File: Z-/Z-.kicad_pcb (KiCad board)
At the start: 4 copper layers, 98 x 98 mm, 138 parts, among them J1 200528-0100, J2 Conn_Coaxial, J3 Conn_Coaxial, J4 200528-0100, J5 Conn_01x02, K1 IM02DGR, Q1 NX3008NBKS, Q10 NX3008NBKS, Q11 IRLML2803, Q12 MBT2222ADW1T1, Q13 IRLML2803, Q14 NX3008NBKS, Q15 IRF7404, Q16 MBT2222ADW1T1, Q17 IRF7404, Q18 IRLML2803, Q19 IRF7404, Q2 NX3008NBKS, Q3 MBT2222ADW1T1, Q4 MBT2222ADW1T1, Q5 NX3008NBKS, Q6 NX3008NBKS, Q7 MBT2222ADW1T1, Q8 MBT2222ADW1T1, Q9 MMBT2222AT, U1 OPT4003DNPRQ1, U2 LTC4316xDD, U3 ADM1176-1ARMZ-R7, U4 NCV891330PD50R2G, U5 DRV8830DRC

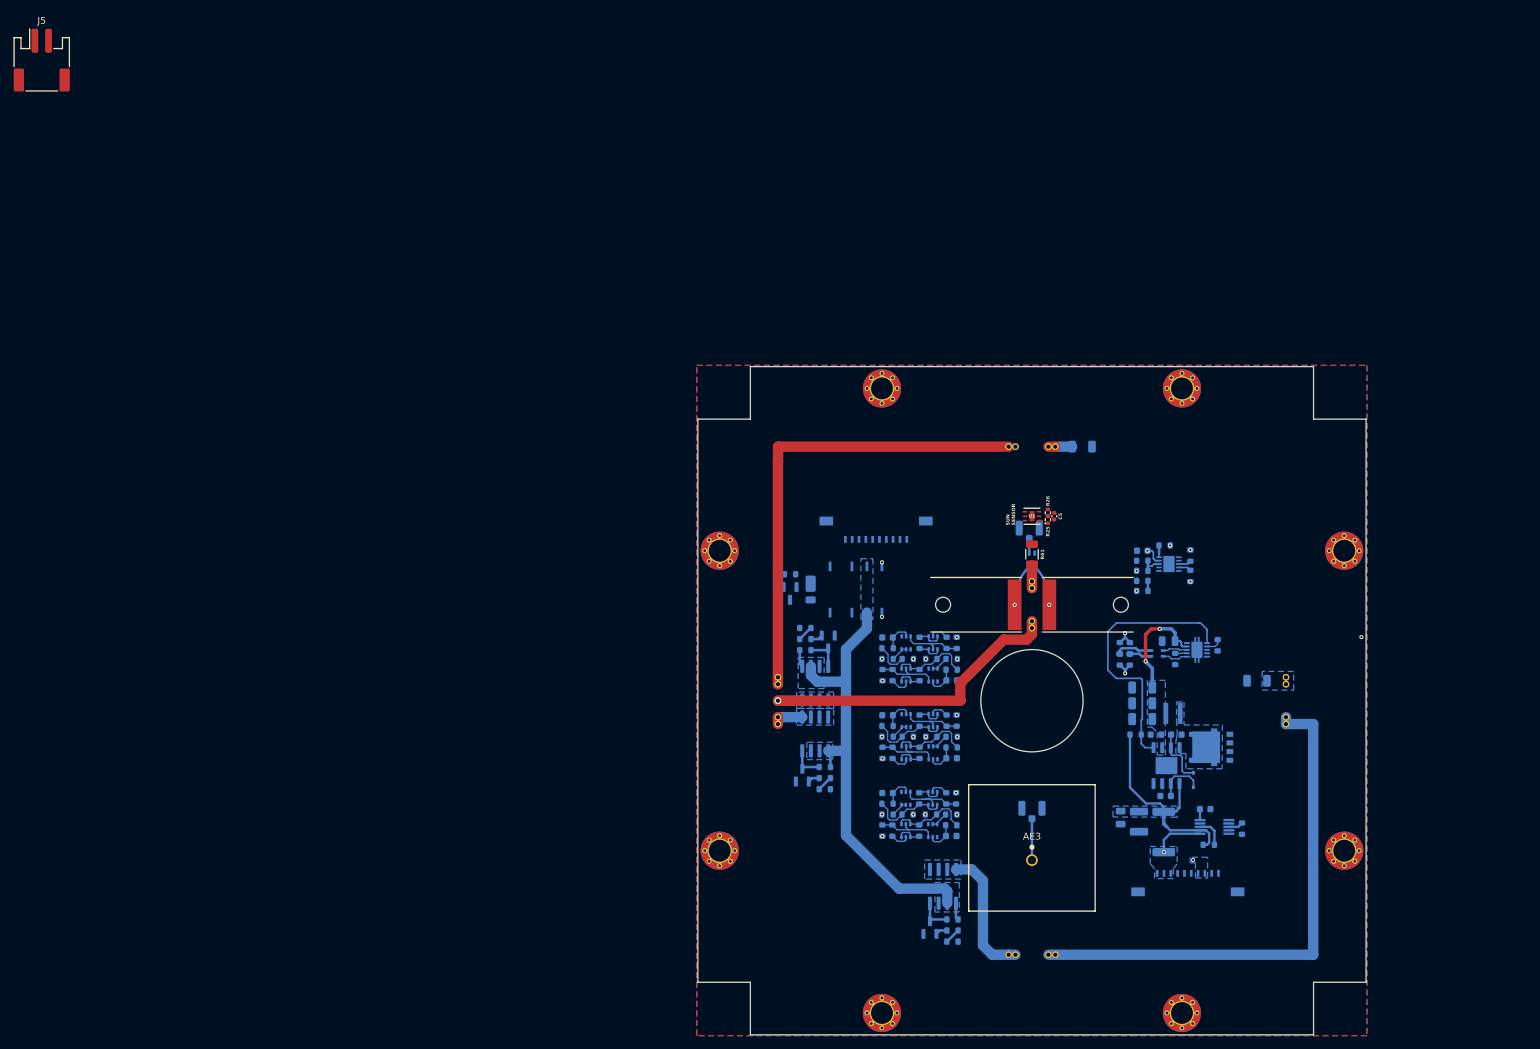
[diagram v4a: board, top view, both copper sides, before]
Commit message: First pass on routing and silkscreen
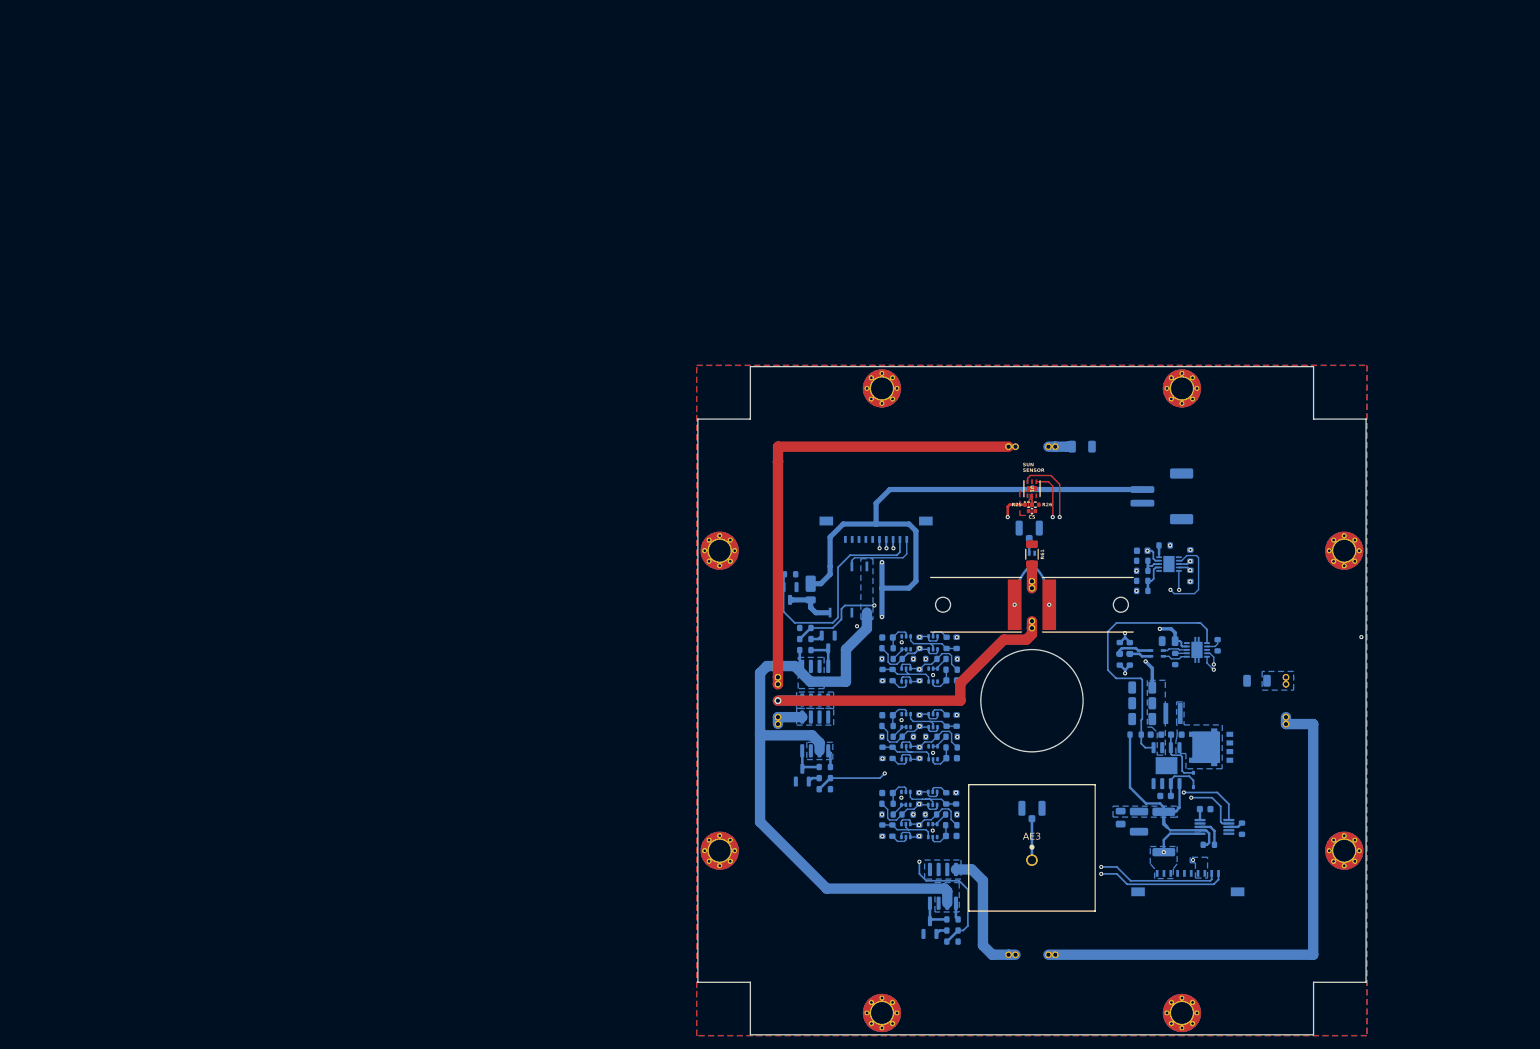
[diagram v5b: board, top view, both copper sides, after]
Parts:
- J5: moved to B.Cu
- moved J5 176.3 mm to (168.9, 69.1), turned to -90 degrees
- moved U1 4.04 mm to (149.9, 68.0), turned to 90 degrees
- moved R25 3.60 mm to (149.4, 70.3), turned to 180 degrees
- moved C5 3.36 mm to (149.9, 71.2), turned to 0 degrees
- moved R26 2.18 mm to (150.4, 70.3), turned to 180 degrees
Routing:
- net SDA: track 11.4 -> 97.3 mm, vias 0 -> 4
- net SCL: track 11.5 -> 90.5 mm, vias 0 -> 4
- net VBATT: track 94.0 -> 172.4 mm
- net BURN_EN2: track 2.32 -> 71.3 mm, vias 0 -> 2
- net SDA_M: track 11.9 -> 70.8 mm, vias 0 -> 2
- net SDA_LS: track 8.67 -> 67.5 mm, vias 0 -> 2
- net SCL_M: track 11.9 -> 69.4 mm, vias 0 -> 2
- net SDA_CPWR: track 11.9 -> 63.6 mm, vias 0 -> 2
- net SCL_CPWR: track 11.9 -> 62.4 mm, vias 0 -> 2
- net SCL_LS: track 11.9 -> 60.2 mm, vias 0 -> 2
- net BURN_EN1: track 2.32 -> 45.4 mm, vias 0 -> 2
- net /I2C Devices/SDAOUT: track 1.86 -> 36.2 mm, vias 0 -> 2
- net BURN_RELAY_A: track 0.00 -> 33.7 mm
- net /I2C Devices/SCLOUT: track 1.86 -> 35.0 mm, vias 0 -> 2
- net /Burn Wires/VBURN_A_IN: track 71.0 -> 98.5 mm
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- added copper zone on F.Cu, net 3.3V
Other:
- board text added: "3.3V"
- board text added: "BURNWIRE 1"
- board text added: "BURNWIRE 2"
- board text added: "BURNWIRE 3"
- board text added: "BURN_EN1"
- board text added: "BURN_EN2"
- board text added: "BURN_EN3"
- board text added: "BURN_EN4"
- board text added: "COIL DRIVER"
- board text added: "COIL PWR MONITOR"
- board text added: "GND"
- board text added: "I2C ADDR TRANSLATOR"
- board text added: "I2C BUS PROTECTION"
- board text added: "MAINBOARD"
- board text added: "POWER RELAY A"
- board text added: "REGULATOR BUCK 5V"
- board text added: "RELAY_A"
- board text added: "SCL"
- board text added: "SDA"
- board text added: "VBATT"

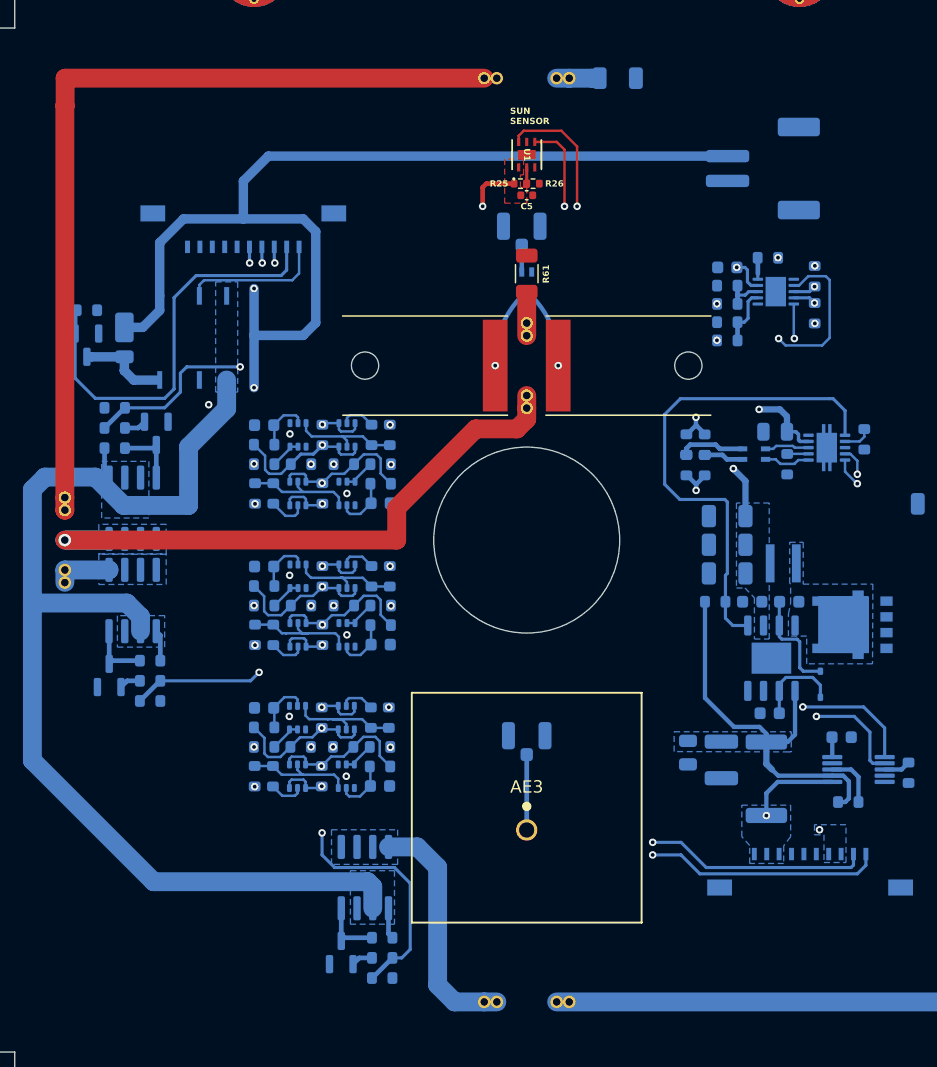
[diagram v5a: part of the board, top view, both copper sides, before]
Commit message: More routing and silkscreen
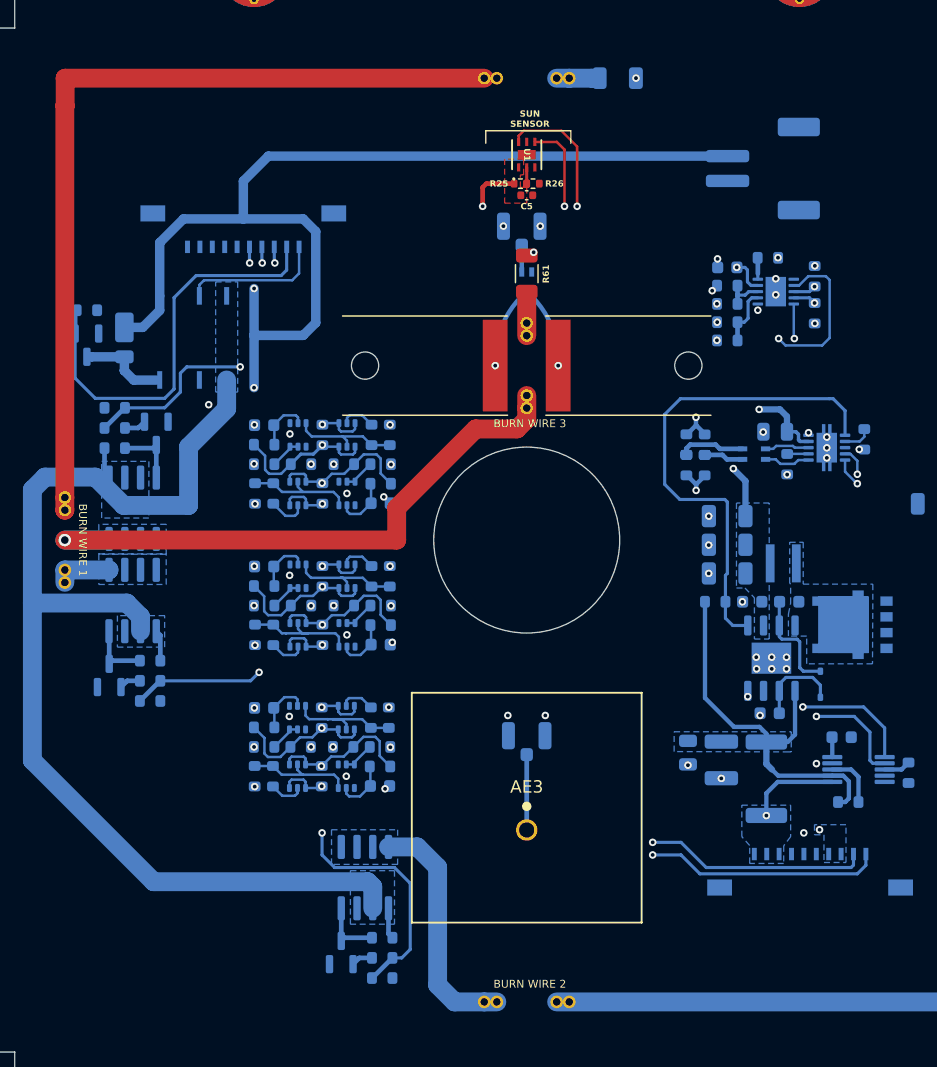
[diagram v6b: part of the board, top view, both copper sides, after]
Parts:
- added G***: LOGO, LOGO, B.Cu at (148.1, 78.4)
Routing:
- net GND: vias 7 -> 48
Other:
- board text added: "ALUN"
- board text added: "ARGUS-1 Cubesat Carnegie Mellon University Z- Solar Panel v1"
- board text added: "BURN WIRE 1"
- board text added: "BURN WIRE 2"
- board text added: "BURN WIRE 3"
- board text added: "GPS ANT"
- board text added: "UHF ANT"

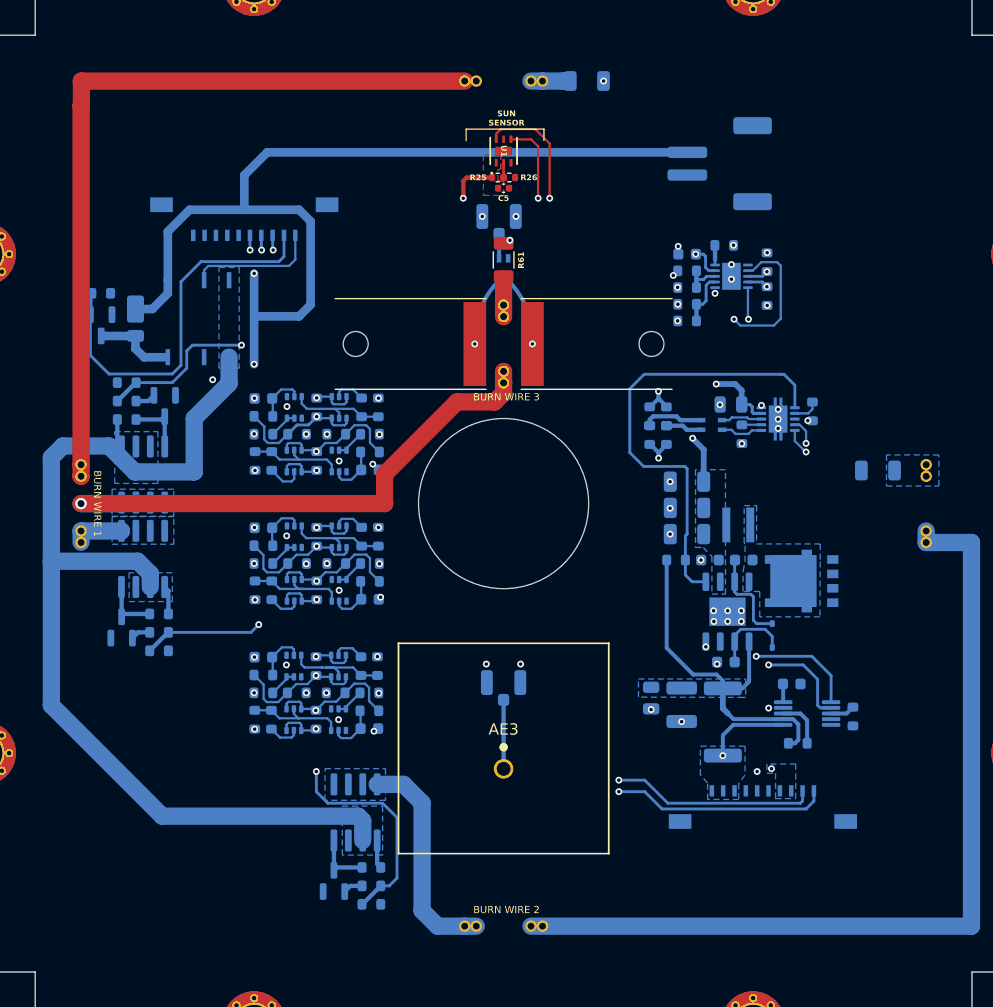
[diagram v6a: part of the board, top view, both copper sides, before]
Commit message: Added stitching vias
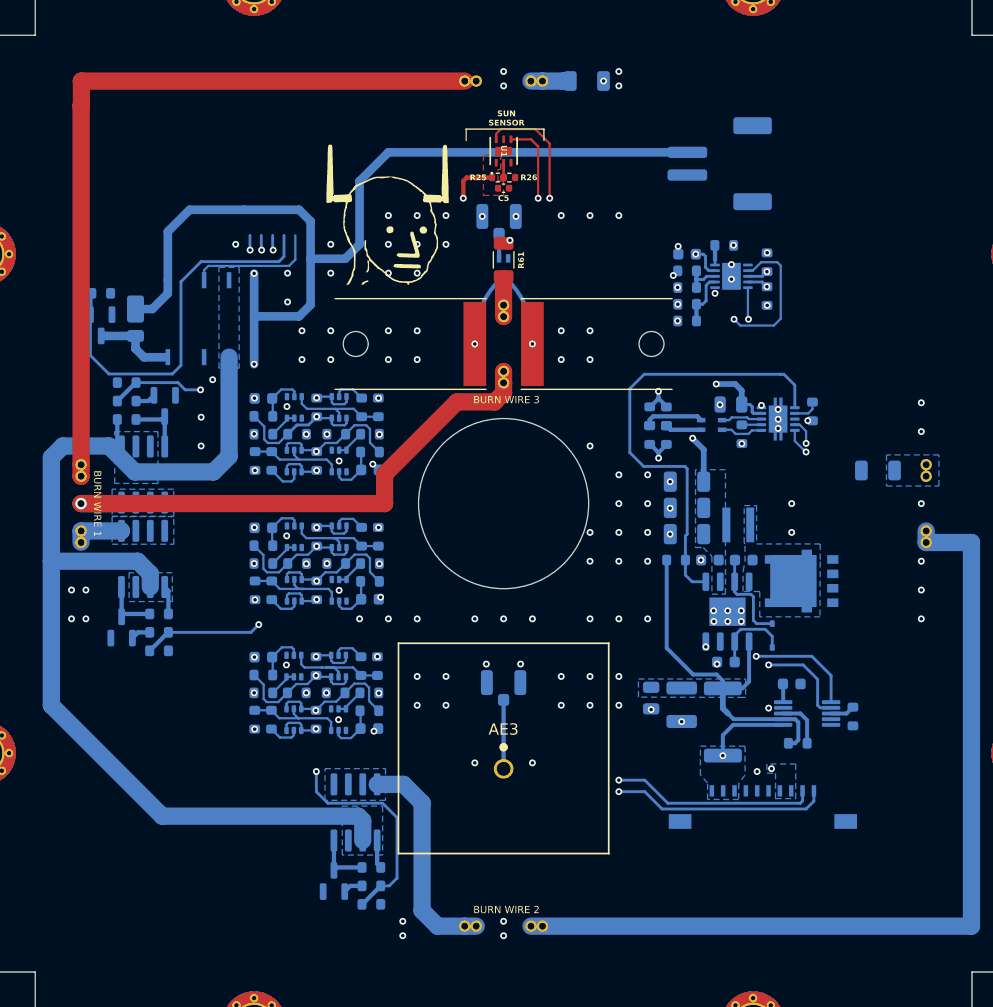
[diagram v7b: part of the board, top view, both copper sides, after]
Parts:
- removed J4: 200528-0100, Connector_FFC-FPC:Molex_200528-0100_1x10-1MP_P1.00mm_Horizontal
- added G***: LOGO, LOGO, F.Cu at (139.7, 73.7)
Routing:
- net VBATT: track 172.4 -> 169.8 mm
- net /Burn Wires/VBURN_A_IN: track 98.5 -> 99.5 mm
- net GND: vias 48 -> 130

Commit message: Added J4 back
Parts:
- added J4: 200528-0100, Connector_FFC-FPC:Molex_200528-0100_1x10-1MP_P1.00mm_Horizontal, B.Cu at (127.0, 74.5)
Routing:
- net GND: vias 130 -> 129
